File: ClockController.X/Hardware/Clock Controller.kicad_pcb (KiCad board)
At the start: 4 copper layers, 63.5 x 44.5 mm, 47 parts, among them J1 UJC-VP-3-SMT-TR, J2 HDR-1X2H, Q1 DMG7430LFG-7, Q2 FDD7N25LZTM, Q3 MMBT2222A-TP, Q4 MMBT2907ALT1G, Q5 MMBT2222A-TP, Q6 MMBT2222A-TP, U1 PIC16F15224-I/SL, U2 AS78L05RTR-E1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

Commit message: Updated some footprints
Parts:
- OLED0: footprint Connector_PinHeader_2.54mm:PinHeader_1x04_P2.54mm_Vertical -> Display_:SSD1306 0.91 128x32 OLED
- turned OLED0 to 0.0010523 degrees
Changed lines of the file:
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@@
 		(embedded_fonts no)
 	)
-	(footprint "Connector_PinHeader_2.54mm:PinHeader_1x04_P2.54mm_Vertical"
+	(footprint "Display_:SSD1306 0.91 128x32 OLED"
 		(layer "B.Cu")
-		(at 144.018 92.202 -179.9989477)
-		(descr "Through hole straight pin header, 1x04, 2.54mm pitch, single row")
-		(tags "Through hole pin header THT 1x04 2.54mm single row")
+		(at 144.018 92.202 0.0010523)
 		(property "Reference" "OLED0"
-			(at 2.57817 -3.799953 90.0010523)
-			(layer "B.SilkS")
-			(effects
-				(font
-					(size 1 1)
-					(thickness 0.15)
+			(at -2 3.81 90.0010523)
+			(unlocked yes)
+			(layer "B.SilkS")
+			(effects
+				(font
+					(size 1 1)
+					(thickness 0.1)
 				)
 				(justify mirror)
@@
 		)
 		(property "Value" "HDR-1X4"
-			(at 0 -9.95 0.0010523)
-			(layer "B.Fab")
-			(effects
-				(font
-					(size 1 1)
-					(thickness 0.15)
-				)
-				(justify mirror)
+			(at 2.54 5.08 180.0010523)
+			(unlocked yes)
+			(layer "B.Fab")
+			(effects
+				(font
+					(size 1 1)
+					(thickness 0.15)
+				)
+				(justify left mirror)
 			)
 		)
@@
 			(effects
 				(font
-					(size 1.27 1.27)
+					(size 1 1)
 					(thickness 0.15)
 				)
@@
 			(effects
 				(font
-					(size 1.27 1.27)
+					(size 1 1)
 					(thickness 0.15)
 				)
@@
 		(attr through_hole)
 		(fp_line
-			(start 1.33 -1.27)
-			(end -1.33 -1.27)
-			(stroke
-				(width 0.12)
-				(type solid)
-			)
-			(layer "B.SilkS")
-		)
-		(fp_line
-			(start 1.33 -8.95)
-			(end 1.33 -1.27)
-			(stroke
-				(width 0.12)
-				(type solid)
-			)
-			(layer "B.SilkS")
-		)
-		(fp_line
-			(start 1.33 -8.95)
-			(end -1.33 -8.95)
-			(stroke
-				(width 0.12)
-				(type solid)
-			)
-			(layer "B.SilkS")
-		)
-		(fp_line
-			(start 0 1.33)
-			(end -1.33 1.33)
-			(stroke
-				(width 0.12)
-				(type solid)
-			)
-			(layer "B.SilkS")
-		)
-		(fp_line
-			(start -1.33 1.33)
-			(end -1.33 0)
-			(stroke
-				(width 0.12)
-				(type solid)
-			)
-			(layer "B.SilkS")
-		)
-		(fp_line
-			(start -1.33 -8.95)
-			(end -1.33 -1.27)
-			(stroke
-				(width 0.12)
-				(type solid)
-			)
-			(layer "B.SilkS")
-		)
-		(fp_line
-			(start 1.8 1.8)
-			(end 1.8 -9.4)
-			(stroke
-				(width 0.05)
-				(type solid)
-			)
-			(layer "B.CrtYd")
-		)
-		(fp_line
-			(start 1.8 -9.4)
-			(end -1.8 -9.4)
-			(stroke
-				(width 0.05)
-				(type solid)
-			)
-			(layer "B.CrtYd")
-		)
-		(fp_line
-			(start -1.8 1.8)
-			(end 1.8 1.8)
-			(stroke
-				(width 0.05)
-				(type solid)
-			)
-			(layer "B.CrtYd")
-		)
-		(fp_line
-			(start -1.8 -9.4)
-			(end -1.8 1.8)
-			(stroke
-				(width 0.05)
-				(type solid)
-			)
-			(layer "B.CrtYd")
-		)
-		(fp_line
-			(start 1.27 1.27)
-			(end -0.635 1.27)
-			(stroke
-				(width 0.1)
-				(type solid)
-			)
-			(layer "B.Fab")
-		)
-		(fp_line
-			(start 1.27 -8.89)
-			(end 1.27 1.27)
-			(stroke
-				(width 0.1)
-				(type solid)
-			)
-			(layer "B.Fab")
-		)
-		(fp_line
-			(start -0.635 1.27)
-			(end -1.27 0.635)
-			(stroke
-				(width 0.1)
-				(type solid)
-			)
-			(layer "B.Fab")
-		)
-		(fp_line
-			(start -1.27 0.635)
-			(end -1.27 -8.89)
-			(stroke
-				(width 0.1)
-				(type solid)
-			)
-			(layer "B.Fab")
-		)
-		(fp_line
-			(start -1.27 -8.89)
-			(end 1.27 -8.89)
-			(stroke
-				(width 0.1)
-				(type solid)
-			)
+			(start -1.33 1.27)
+			(end -1.33 8.95)
+			(stroke
+				(width 0.12)
+				(type solid)
+			)
+			(layer "B.SilkS")
+		)
+		(fp_line
+			(start 1.33 -1.33)
+			(end 0 -1.33)
+			(stroke
+				(width 0.12)
+				(type solid)
+			)
+			(layer "B.SilkS")
+		)
+		(fp_line
+			(start 1.33 0)
+			(end 1.33 -1.33)
+			(stroke
+				(width 0.12)
+				(type solid)
+			)
+			(layer "B.SilkS")
+		)
+		(fp_line
+			(start 1.33 1.27)
+			(end -1.33 1.27)
+			(stroke
+				(width 0.12)
+				(type solid)
+			)
+			(layer "B.SilkS")
+		)
+		(fp_line
+			(start 1.33 1.27)
+			(end 1.33 8.95)
+			(stroke
+				(width 0.12)
+				(type solid)
+			)
+			(layer "B.SilkS")
+		)
+		(fp_line
+			(start 1.33 8.95)
+			(end -1.33 8.95)
+			(stroke
+				(width 0.12)
+				(type solid)
+			)
+			(layer "B.SilkS")
+		)
+		(fp_line
+			(start -1.8 -1.8)
+			(end 1.8 -1.8)
+			(stroke
+				(width 0.05)
+				(type solid)
+			)
+			(layer "B.CrtYd")
+		)
+		(fp_line
+			(start -1.8 9.4)
+			(end -1.8 -1.8)
+			(stroke
+				(width 0.05)
+				(type solid)
+			)
+			(layer "B.CrtYd")
+		)
+		(fp_line
+			(start 1.8 -1.8)
+			(end 1.8 9.4)
+			(stroke
+				(width 0.05)
+				(type solid)
+			)
+			(layer "B.CrtYd")
+		)
+		(fp_line
+			(start 1.8 9.4)
+			(end -1.8 9.4)
+			(stroke
+				(width 0.05)
+				(type solid)
+			)
+			(layer "B.CrtYd")
+		)
+		(fp_line
+			(start -1.27 -1.27)
+			(end -1.27 8.89)
+			(stroke
+				(width 0.1)
+				(type solid)
+			)
+			(layer "B.Fab")
+		)
+		(fp_line
+			(start -1.27 8.89)
+			(end 1.27 8.89)
+			(stroke
+				(width 0.1)
+				(type solid)
+			)
+			(layer "B.Fab")
+		)
+		(fp_line
+			(start 0.635 -1.27)
+			(end -1.27 -1.27)
+			(stroke
+				(width 0.1)
+				(type solid)
+			)
+			(layer "B.Fab")
+		)
+		(fp_line
+			(start 1.27 -0.635)
+			(end 0.635 -1.27)
+			(stroke
+				(width 0.1)
+				(type solid)
+			)
+			(layer "B.Fab")
+		)
+		(fp_line
+			(start 1.27 8.89)
+			(end 1.27 -0.635)
+			(stroke
+				(width 0.1)
+				(type solid)
+			)
+			(layer "B.Fab")
+		)
+		(fp_poly
+			(pts
+				(xy -1.778 9.8425) (xy 36.322 9.8425) (xy 36.322 -2.2225) (xy -1.778 -2.2225)
+			)
+			(stroke
+				(width 0.1)
+				(type default)
+			)
+			(fill no)
 			(layer "B.Fab")
 		)
 		(fp_text user "${REFERENCE}"
-			(at 0 -3.81 90.0010523)
-			(layer "B.Fab")
-			(effects
-				(font
-					(size 1 1)
-					(thickness 0.15)
-				)
-				(justify mirror)
+			(at 2.54 2.62 180.0010523)
+			(unlocked yes)
+			(layer "B.Fab")
+			(effects
+				(font
+					(size 1 1)
+					(thickness 0.15)
+				)
+				(justify left mirror)
 			)
 		)
@@
 		)
 		(pad "2" thru_hole oval
-			(at 0 -2.54 180.0010523)
+			(at 0 2.54 180.0010523)
 			(size 1.7 1.7)
 			(drill 1)
@@
 		)
 		(pad "3" thru_hole oval
-			(at 0 -5.08 180.0010523)
+			(at 0 5.08 180.0010523)
 			(size 1.7 1.7)
 			(drill 1)
@@
 		)
 		(pad "4" thru_hole oval
-			(at 0 -7.62 180.0010523)
+			(at 0 7.62 180.0010523)
 			(size 1.7 1.7)
 			(drill 1)
@@
 		)
 		(embedded_fonts no)
-		(model "${KICAD8_3DMODEL_DIR}/Connector_PinHeader_2.54mm.3dshapes/PinHeader_1x04_P2.54mm_Vertical.wrl"
+		(model "${REPO}/3d/0.91in OLED.step"
 			(offset
-				(xyz 0 0 0)
+				(xyz 16.3322 2.3876 1.905)
 			)
 			(scale

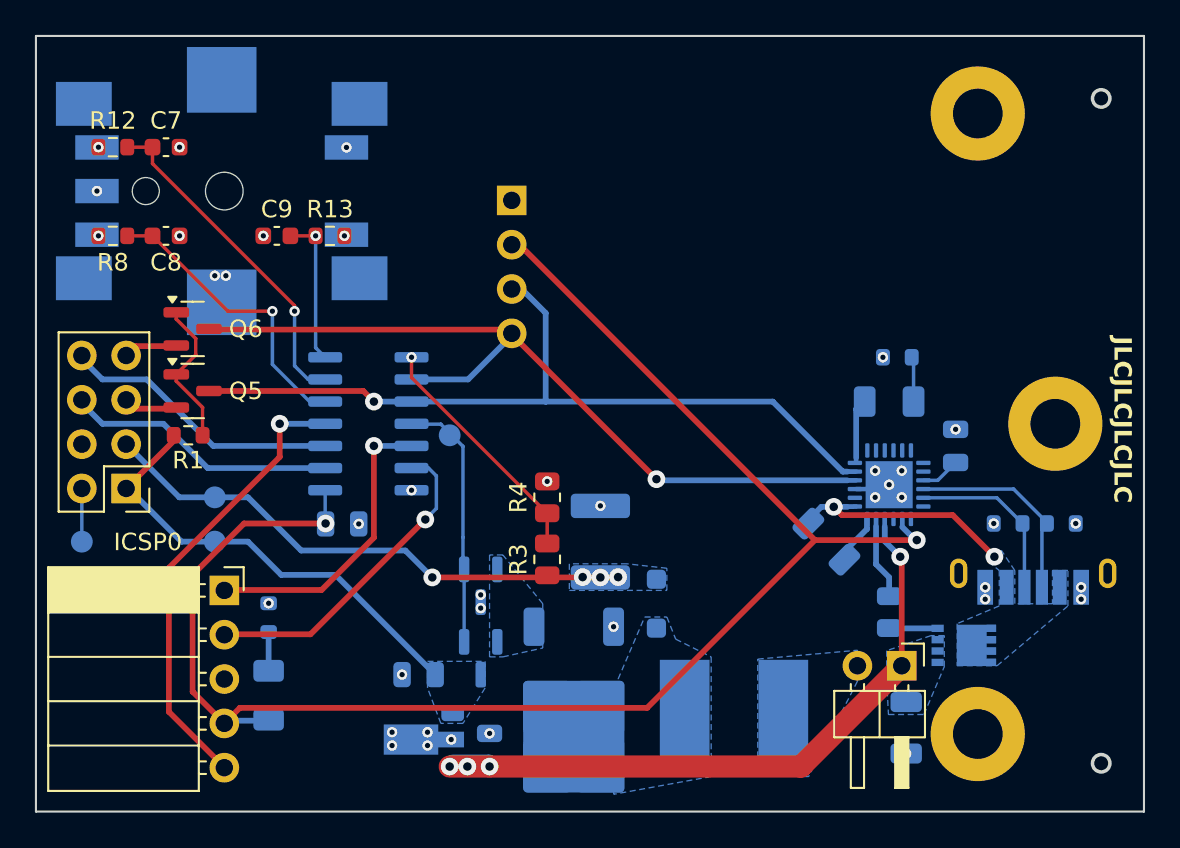
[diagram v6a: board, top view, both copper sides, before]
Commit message: Fixed bad pull-up design of I2C cutoff transistors
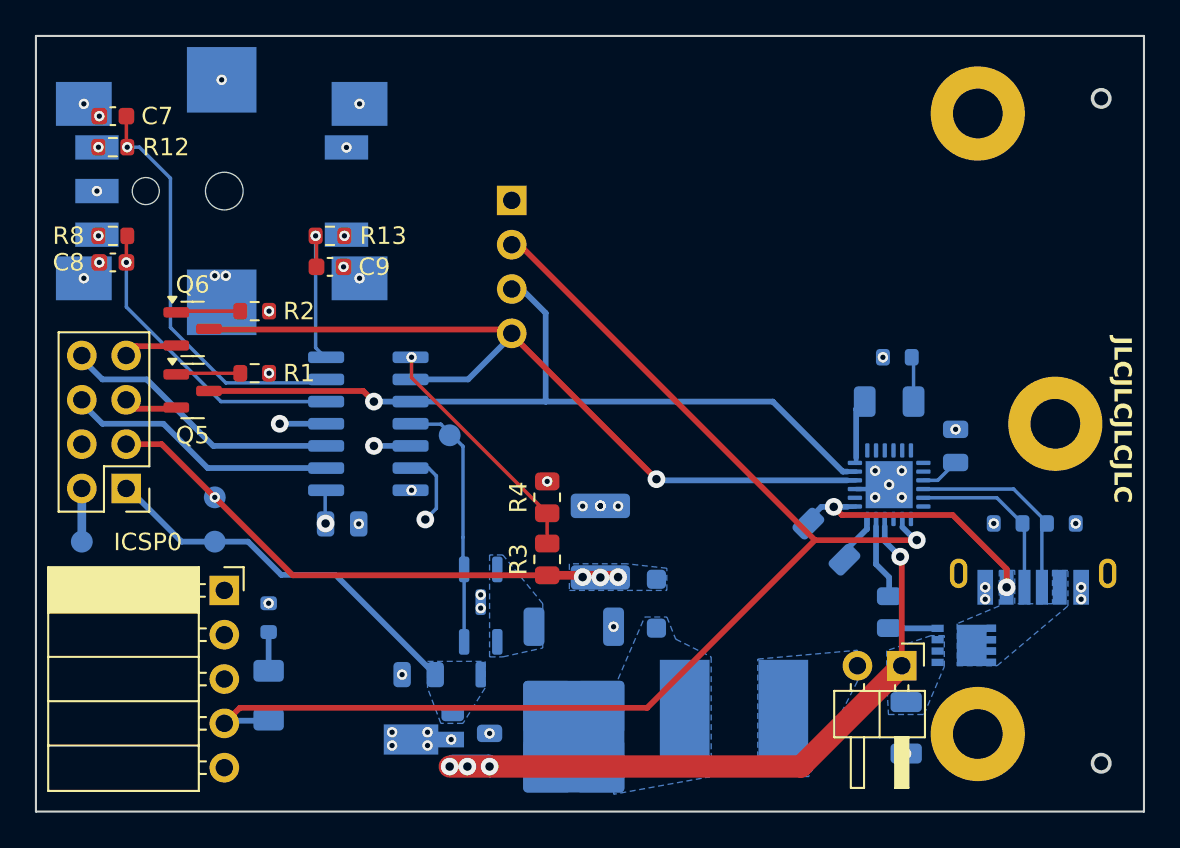
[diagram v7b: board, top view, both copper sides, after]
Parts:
- added R2: 2.2k, Resistor_SMD:R_0603_1608Metric, F.Cu at (129.3, 98.6)
- U1: footprint Package_SO:SOIC-14_3.9x8.7mm_P1.27mm -> Clock Controller:SOIC14P127_869X599X175L84X42N
- moved R1 5.21 mm to (129.3, 102.1), turned to 0.001 degrees
- moved C9 3.53 mm to (133.6, 96.0), turned to 0 degrees
- moved C7 3.53 mm to (121.2, 87.4), turned to 180 degrees
- moved C8 3.41 mm to (121.2, 95.8), turned to 0 degrees
- turned U1 to 90 degrees
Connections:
- Q6 pad 1: Net-(Q5-B) -> Net-(Q6-B)
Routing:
- net +5V: track 26.3 -> 36.6 mm, vias 0 -> 2
- net Net-(Q5-B): track 8.60 -> 3.70 mm
- net Rotary_B: track 19.4 -> 23.9 mm
- net Net-(Q6-B): track 0.00 -> 3.70 mm
- net VBUS: track 13.2 -> 15.3 mm
- net Rotary_A: track 17.1 -> 17.7 mm
- net GND: vias 36 -> 46

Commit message: Updated version number on board
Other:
- board text added: "Nixie Clock Controller (v1.1.3) Aaron Johnson 4/14/2026"
- board text removed: "Nixie Clock Controller (v1.1) Aaron Johnson 4/4/2026"
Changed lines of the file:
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@@
 		)
 	)
-	(gr_text "Nixie Clock Controller (v1.1)\nAaron Johnson\n4/4/2026"
-		(at 156.5721 84.0486 0)
+	(gr_text "Nixie Clock Controller (v1.1.3)\nAaron Johnson\n4/14/2026"
+		(at 165.1 84.328 0)
 		(layer "B.SilkS")
 		(effects
